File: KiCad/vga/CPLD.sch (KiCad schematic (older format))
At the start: 27 parts, among them U1 EPM7128S, U14 EPM7064S, X1 50 MHz

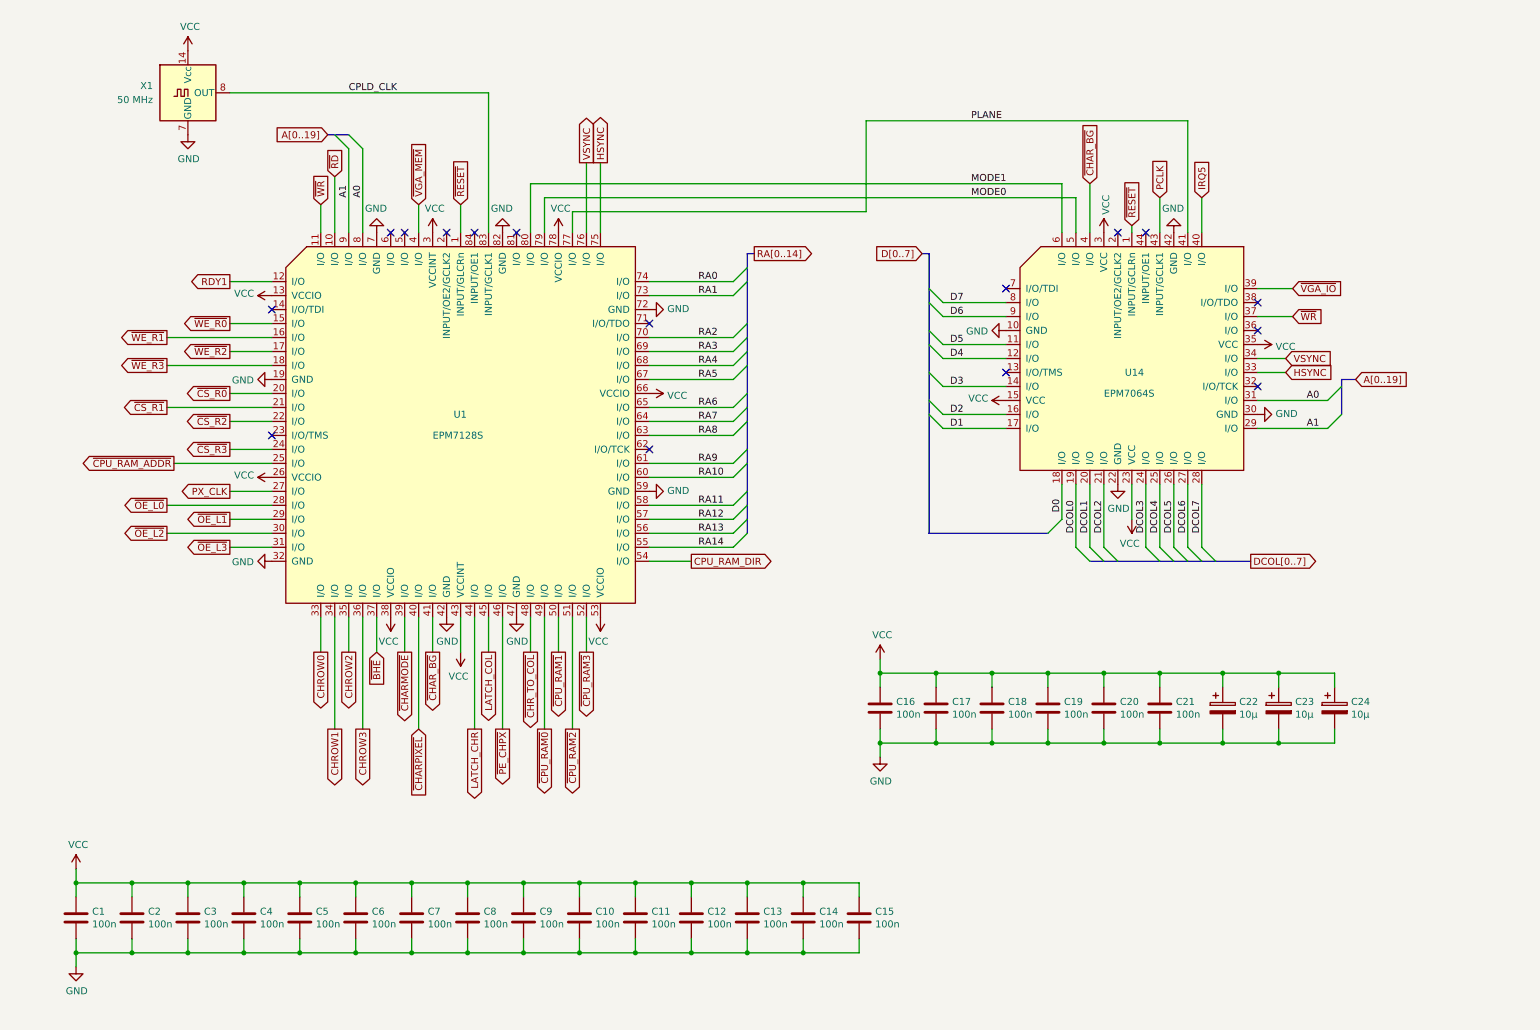
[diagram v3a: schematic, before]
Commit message: Replaced MAX7000 CPLD with MAX II in graphics adapter. PCB redesign with smaller size.
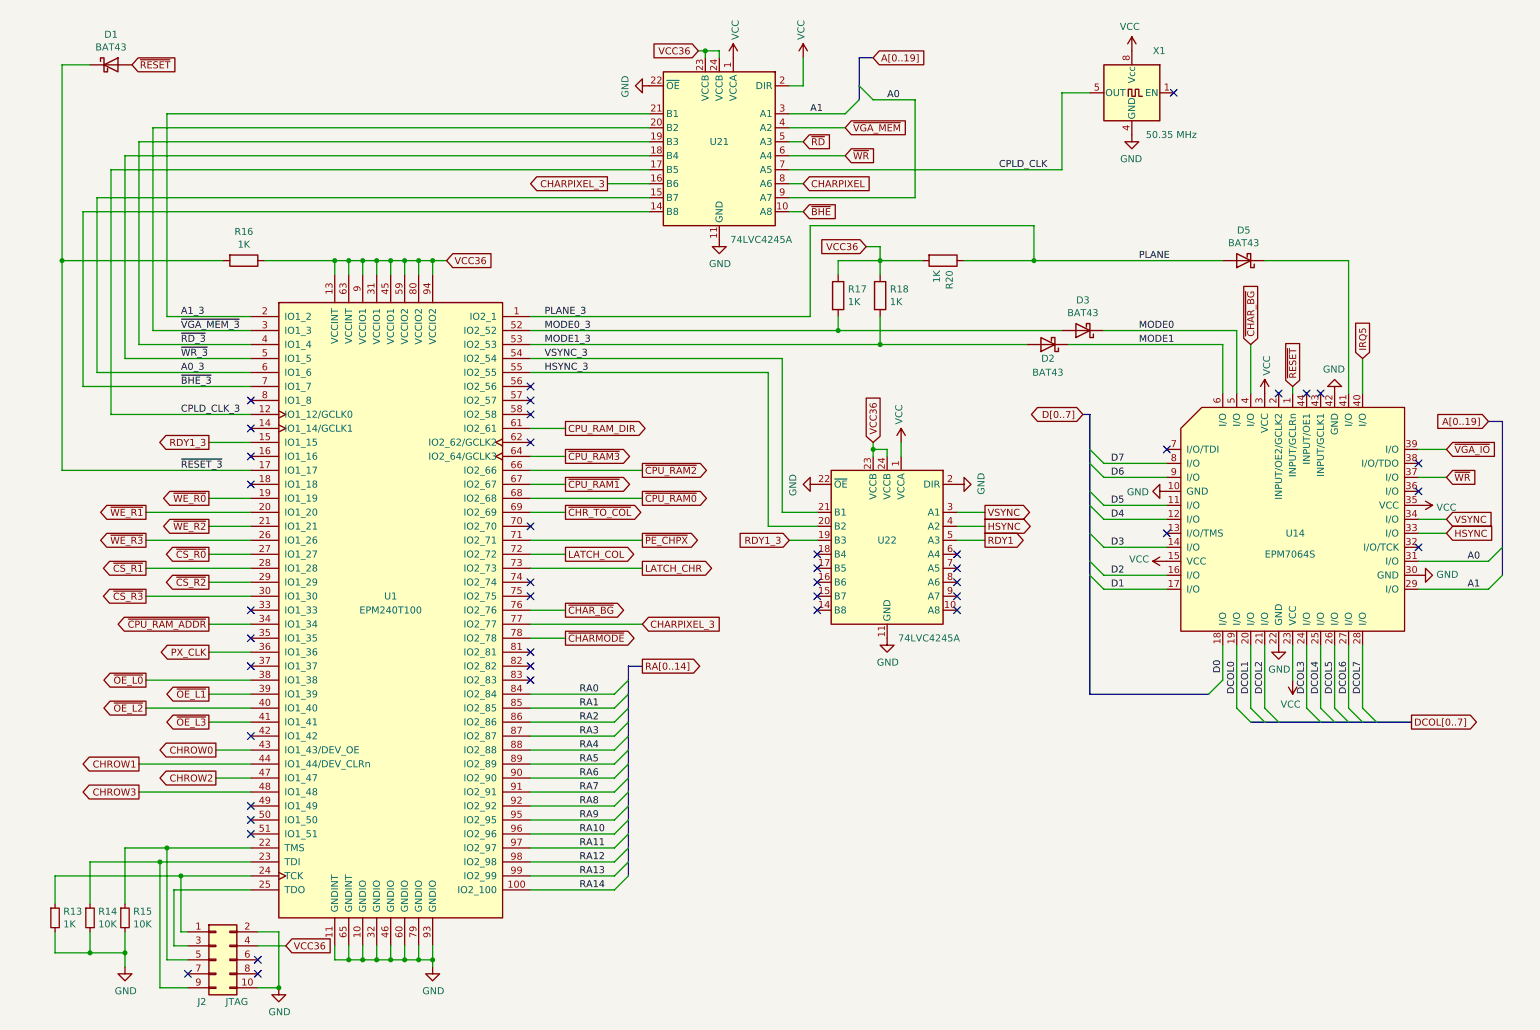
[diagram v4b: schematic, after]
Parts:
- removed C1, C10, C11, C12, C13, C14, C15, C17, C2, C21, C3, C4, C5, C6, C7, C8, C9: 100n, Capacitor_THT:C_Disc_D4.3mm_W1.9mm_P5.00mm, symbol Device:C
- removed C16, C18, C19, C20: 100n, Capacitor_THT:C_Disc_D3.4mm_W2.1mm_P2.50mm, symbol Device:C
- removed C22, C23, C24: 10µ, Capacitor_THT:CP_Radial_D5.0mm_P2.50mm, symbol Device:CP
- removed U1: EPM7128S, Package_LCC:PLCC-84_THT-Socket, symbol Mini8086:EPM7128S
- removed X1: 50 MHz, Oscillator:Oscillator_DIP-14, symbol Oscillator:ACO-xxxMHz
- added D1, D2, D3, D5: BAT43, Diode_THT:D_DO-34_SOD68_P2.54mm_Vertical_KathodeUp, symbol Device:D_Schottky
- added J2: JTAG, Connector_IDC:IDC-Header_2x05_P2.54mm_Vertical, symbol Connector_Generic:Conn_02x05_Odd_Even
- added R13: 1K, Resistor_THT:R_Axial_DIN0207_L6.3mm_D2.5mm_P2.54mm_Vertical, symbol Device:R_Small
- added R14, R15: 10K, Resistor_THT:R_Axial_DIN0207_L6.3mm_D2.5mm_P2.54mm_Vertical, symbol Device:R_Small
- added R16, R17, R18, R20: 1K, Resistor_THT:R_Axial_DIN0207_L6.3mm_D2.5mm_P2.54mm_Vertical, symbol Device:R
- added U1: EPM240T100, Package_QFP:LQFP-100_14x14mm_P0.5mm, symbol CPLD_Altera:EPM240T100
- added U21, U22: 74LVC4245A, Package_SO:TSSOP-24_4.4x7.8mm_P0.65mm, symbol Logic_LevelTranslator:SN74AVC8T245PW
- added X1: 50.35 MHz, Oscillator:Oscillator_DIP-8, symbol Oscillator:CXO_DIP8
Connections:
- net A0: now also U21.9 (A7)
- net A1: now also U21.3 (A1)
- net CHROW0: now also U1.43 (IO1_43/DEV_OE)
- net CHROW1: now also U1.44 (IO1_44/DEV_CLRn)
- net CHROW2: now also U1.47 (IO1_47)
- net CHROW3: now also U1.48 (IO1_48)
- net CPLD_CLK: now also U21.7 (A5), X1.5 (OUT)
- net CPU_RAM_DIR: now also U1.61 (IO2_61)
- net GND: now also J2.10 (Pin_10), J2.2 (Pin_2), R13.2, R14.2, R15.2, U1.10 (GNDIO), U1.11 (GNDINT), U1.32 (GNDIO), U1.46 (GNDIO), U1.60 (GNDIO), U1.65 (GNDINT), U1.79 (GNDIO), U1.93 (GNDIO), U21.11 (GND), U21.12 (GND), U21.13 (GND), U21.22 (~OE), U22.11 (GND), U22.12 (GND), U22.13 (GND), U22.2 (DIR), U22.22 (~OE), X1.4 (GND)
- net HSYNC: now also U22.4 (A2)
- net LATCH_CHR: now also U1.73 (IO2_73)
- net LATCH_COL: now also U1.72 (IO2_72)
- net MODE0: now also D3.1 (K)
- net MODE1: now also D2.1 (K)
- net PLANE: now also D5.2 (A), R20.1, U1.1 (IO2_1); no longer U14.41 (I/O)
- net PX_CLK: now also U1.36 (IO1_36)
- net RA0: now also U1.84 (IO2_84)
- net RA1: now also U1.85 (IO2_85)
- net RA10: now also U1.96 (IO2_96)
- net RA11: now also U1.97 (IO2_97)
- net RA12: now also U1.98 (IO2_98)
- net RA13: now also U1.99 (IO2_99)
- net RA14: now also U1.100 (IO2_100)
- net RA2: now also U1.86 (IO2_86)
- net RA3: now also U1.87 (IO2_87)
- net RA4: now also U1.88 (IO2_88)
- net RA5: now also U1.89 (IO2_89)
- net RA6: now also U1.90 (IO2_90)
- net RA7: now also U1.91 (IO2_91)
- net RA8: now also U1.92 (IO2_92)
- net RA9: now also U1.95 (IO2_95)
- net RDY1: now also U22.5 (A3)
- net VCC: now also U21.1 (VCCA), U21.2 (DIR), U22.1 (VCCA), X1.8 (Vcc)
- net VSYNC: now also U22.3 (A1)
- net ~BHE: now also U21.10 (A8)
- net ~CHARMODE: now also U1.78 (IO2_78)
- net ~CHAR_BG: now also U1.76 (IO2_76)
- net ~CHR_TO_COL: now also U1.69 (IO2_69)
- net ~CPU_RAM0: now also U1.68 (IO2_68)
- net ~CPU_RAM1: now also U1.67 (IO2_67)
- net ~CPU_RAM2: now also U1.66 (IO2_66)
- net ~CPU_RAM3: now also U1.64 (IO2_64/GCLK3)
- net ~CPU_RAM_ADDR: now also U1.34 (IO1_34)
- net ~CS_R0: now also U1.27 (IO1_27)
- net ~CS_R1: now also U1.28 (IO1_28)
- net ~CS_R2: now also U1.29 (IO1_29)
- net ~CS_R3: now also U1.30 (IO1_30)
- net ~OE_L0: now also U1.38 (IO1_38)
- net ~OE_L1: now also U1.39 (IO1_39)
- net ~OE_L2: now also U1.40 (IO1_40)
- net ~OE_L3: now also U1.41 (IO1_41)
- net ~PE_CHPX: now also U1.71 (IO2_71)
- net ~RD: now also U21.5 (A3)
- net ~RESET: now also D1.2 (A)
- net ~VGA_MEM: now also U21.4 (A2)
- net ~WE_R0: now also U1.19 (IO1_19)
- net ~WE_R1: now also U1.20 (IO1_20)
- net ~WE_R2: now also U1.21 (IO1_21)
- net ~WE_R3: now also U1.26 (IO1_26)
- net ~WR: now also U21.6 (A4)
- net PCLK: no longer names the net of U14.43 (INPUT/GCLK1)
- new net: D5.1 (K), U14.41 (I/O)
- new net: J2.5 (Pin_5), R15.1, U1.22 (TMS)
- new net: J2.9 (Pin_9), R14.1, U1.23 (TDI)
- new net: J2.1 (Pin_1), R13.1, U1.24 (TCK)
- new net: J2.3 (Pin_3), U1.25 (TDO)
- new net A0_3: U1.6 (IO1_6), U21.15 (B7)
- new net A1_3: U1.2 (IO1_2), U21.21 (B1)
- new net CHARPIXEL: U21.8 (A6)
- new net CHARPIXEL_3: U1.77 (IO2_77), U21.16 (B6)
- new net CPLD_CLK_3: U1.12 (IO1_12/GCLK0), U21.17 (B5)
- new net HSYNC_3: U1.55 (IO2_55), U22.20 (B2)
- new net MODE0_3: D3.2 (A), R17.2, U1.52 (IO2_52)
- new net MODE1_3: D2.2 (A), R18.2, U1.53 (IO2_53)
- new net RDY1_3: U1.15 (IO1_15), U22.19 (B3)
- new net VCC36: J2.4 (Pin_4), R16.1, R17.1, R18.1, R20.2, U1.13 (VCCINT), U1.31 (VCCIO1), U1.45 (VCCIO1), U1.59 (VCCIO2), U1.63 (VCCINT), U1.80 (VCCIO2), U1.9 (VCCIO1), U1.94 (VCCIO2), U21.23 (VCCB), U21.24 (VCCB), U22.23 (VCCB), U22.24 (VCCB)
- new net VSYNC_3: U1.54 (IO2_54), U22.21 (B1)
- new net ~BHE_3: U1.7 (IO1_7), U21.14 (B8)
- new net ~RD_3: U1.4 (IO1_4), U21.19 (B3)
- new net ~RESET_3: D1.1 (K), R16.2, U1.17 (IO1_17)
- new net ~VGA_MEM_3: U1.3 (IO1_3), U21.20 (B2)
- new net ~WR_3: U1.5 (IO1_5), U21.18 (B4)
- no-connect marks 16 -> 43
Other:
- moved on the sheet: U14

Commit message: Finished VGA adapter Rev. 1.0
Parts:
- removed U22: 74LVC4245A, Package_SO:TSSOP-24_4.4x7.8mm_P0.65mm, symbol Logic_LevelTranslator:SN74AVC8T245PW
- added JP1: CHARPIXEL, Jumper:SolderJumper-3_P1.3mm_Open_RoundedPad1.0x1.5mm_NumberLabels, symbol Jumper:Jumper_3_Bridged12
- added U22: 74ACT32, Package_SO:SOIC-14_3.9x8.7mm_P1.27mm, symbol 74xx:74LS32
- R13: value 1K -> 2K2
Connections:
- net CHARPIXEL: now also JP1.1 (A)
- net CHARPIXEL_3: now also JP1.3 (B); no longer U1.77 (IO2_77)
- net CHROW0: now also U1.47 (IO1_47); no longer U1.43 (IO1_43/DEV_OE)
- net CHROW1: now also U1.48 (IO1_48); no longer U1.44 (IO1_44/DEV_CLRn)
- net CHROW2: now also U1.49 (IO1_49); no longer U1.47 (IO1_47)
- net CHROW3: now also U1.50 (IO1_50); no longer U1.48 (IO1_48)
- net GND: now also U22.12, U22.13, U22.7 (GND); no longer R14.2, R15.2
- net HSYNC: now also U22.6
- net HSYNC_3: now also U22.4, U22.5
- net PLANE: now also D5.1 (K), U14.41 (I/O); no longer D5.2 (A), R20.1, U1.1 (IO2_1)
- net RDY1: now also U22.8
- net VCC: now also U22.14 (VCC)
- net VCC36: now also R14.2, R15.2
- net VSYNC: now also U22.3
- net VSYNC_3: now also U22.1, U22.2
- net ~RESET_3: now also U1.44 (IO1_44/DEV_CLRn); no longer U1.17 (IO1_17)
- net ~VGA_MEM: now also U22.10
- net TMS: now reaches J2.5 (Pin_5), R15.1, U1.22 (TMS)
- net TDI: now reaches J2.9 (Pin_9), R14.1, U1.23 (TDI)
- net TCK: now reaches J2.1 (Pin_1), R13.1, U1.24 (TCK)
- net TDO: now reaches J2.3 (Pin_3), U1.25 (TDO)
- net RDY1_3 renamed ~BLOCK_CPU
- net ~BLOCK_CPU: now also U22.9
- new net CHARPIXEL_CPLD: JP1.2 (C), U1.77 (IO2_77)
- new net PLANE_3: D5.2 (A), R20.1, U1.1 (IO2_1)
- no-connect marks 43 -> 34
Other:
- moved on the sheet: D2, D3, D5
